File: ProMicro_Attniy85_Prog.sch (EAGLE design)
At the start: 4 parts, among them U1 ATTINY85-20P

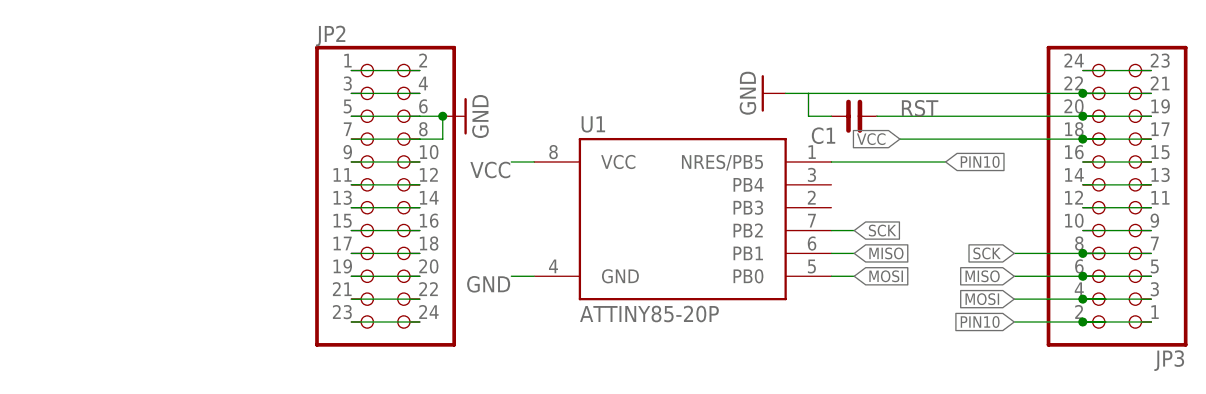
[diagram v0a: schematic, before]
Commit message: Add files via upload
LEDs added following the desing in [Utiliza tu placa Arduino como programador para ATtiny]https://fabricadigital.org/tutoriales/utiliza-tu-placa-arduino-como-programador-para-attiny/
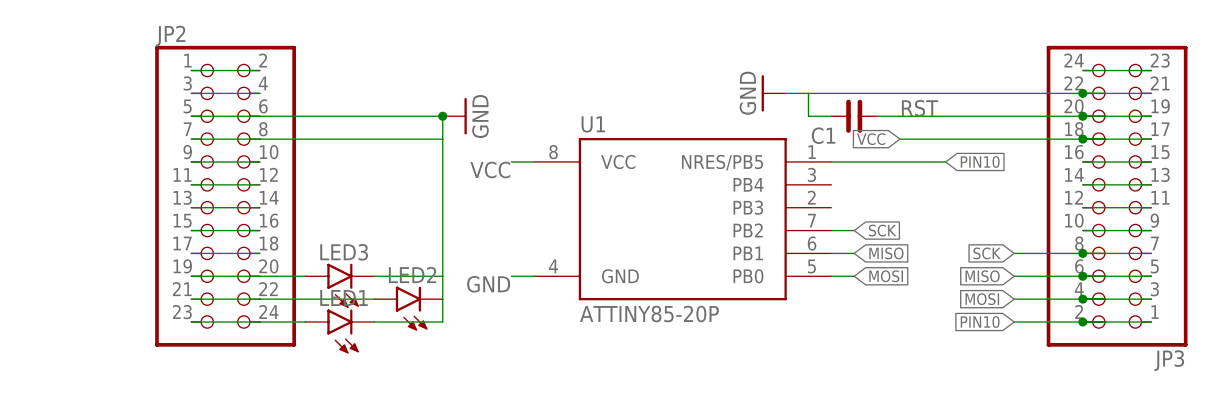
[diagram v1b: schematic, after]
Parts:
- added LED1, LED2, LED3: (no value), led:LEDCHIP-LED0805
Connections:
- removed net N$10: JP2.23, JP2.24
- removed net N$8: JP2.19, JP2.20
- removed net N$9: JP2.21, JP2.22
- new net PIN7: JP2.19, JP2.20, LED3.A
- new net PIN8: JP2.21, JP2.22, LED2.A
- new net PIN9: JP2.23, JP2.24, LED1.A
- net GND: now also LED1.C, LED2.C, LED3.C
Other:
- moved on the sheet: JP2
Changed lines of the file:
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@@
 <part name="JP2" library="pinhead" library_urn="urn:adsk.eagle:library:325" deviceset="PINHD-2X12" device="" package3d_urn="urn:adsk.eagle:package:22420/2"/>
 <part name="JP3" library="pinhead" library_urn="urn:adsk.eagle:library:325" deviceset="PINHD-2X12" device="" package3d_urn="urn:adsk.eagle:package:22420/2"/>
+<part name="LED1" library="led" library_urn="urn:adsk.eagle:library:259" deviceset="LED" device="CHIP-LED0805" package3d_urn="urn:adsk.eagle:package:15818/2"/>
+<part name="LED2" library="led" library_urn="urn:adsk.eagle:library:259" deviceset="LED" device="CHIP-LED0805" package3d_urn="urn:adsk.eagle:package:15818/2"/>
+<part name="LED3" library="led" library_urn="urn:adsk.eagle:library:259" deviceset="LED" device="CHIP-LED0805" package3d_urn="urn:adsk.eagle:package:15818/2"/>
 </parts>
 <sheets>
@@
 <attribute name="VALUE" x="57.15" y="23.8125" size="1.778" layer="96"/>
 </instance>
-<instance part="JP2" gate="A" x="7.62" y="20.32" smashed="yes">
-<attribute name="NAME" x="1.27" y="36.195" size="1.778" layer="95"/>
-<attribute name="VALUE" x="1.27" y="0" size="1.778" layer="96"/>
+<instance part="JP2" gate="A" x="-10.16" y="20.32" smashed="yes">
+<attribute name="NAME" x="-16.51" y="36.195" size="1.778" layer="95"/>
+<attribute name="VALUE" x="-16.51" y="0" size="1.778" layer="96"/>
 </instance>
 <instance part="JP3" gate="A" x="91.44" y="17.78" smashed="yes" rot="R180">
 <attribute name="NAME" x="97.79" y="1.905" size="1.778" layer="95" rot="R180"/>
 <attribute name="VALUE" x="97.79" y="38.1" size="1.778" layer="96" rot="R180"/>
+</instance>
+<instance part="LED1" gate="G$1" x="2.54" y="5.08" smashed="yes" rot="R90">
+<attribute name="NAME" x="7.112" y="8.636" size="1.778" layer="95" rot="R180"/>
+<attribute name="VALUE" x="7.112" y="10.795" size="1.778" layer="96" rot="R180"/>
+</instance>
+<instance part="LED2" gate="G$1" x="10.16" y="7.62" smashed="yes" rot="R90">
+<attribute name="NAME" x="14.732" y="11.176" size="1.778" layer="95" rot="R180"/>
+<attribute name="VALUE" x="14.732" y="13.335" size="1.778" layer="96" rot="R180"/>
+</instance>
+<instance part="LED3" gate="G$1" x="2.54" y="10.16" smashed="yes" rot="R90">
+<attribute name="NAME" x="7.112" y="13.716" size="1.778" layer="95" rot="R180"/>
+<attribute name="VALUE" x="7.112" y="15.875" size="1.778" layer="96" rot="R180"/>
 </instance>
 </instances>
@@
 <net name="GND" class="0">
 <segment>
-<wire x1="12.7" y1="27.94" x2="15.24" y2="27.94" width="0.1524" layer="91"/>
+<wire x1="-5.08" y1="27.94" x2="15.24" y2="27.94" width="0.1524" layer="91"/>
 <wire x1="15.24" y1="27.94" x2="15.24" y2="25.4" width="0.1524" layer="91"/>
 <pinref part="GND2" gate="1" pin="GND"/>
@@
 <pinref part="JP2" gate="A" pin="6"/>
 <pinref part="JP2" gate="A" pin="8"/>
-<wire x1="12.7" y1="25.4" x2="15.24" y2="25.4" width="0.1524" layer="91"/>
+<wire x1="-5.08" y1="25.4" x2="15.24" y2="25.4" width="0.1524" layer="91"/>
 <pinref part="JP2" gate="A" pin="5"/>
-<wire x1="5.08" y1="27.94" x2="12.7" y2="27.94" width="0.1524" layer="91"/>
+<wire x1="-12.7" y1="27.94" x2="-5.08" y2="27.94" width="0.1524" layer="91"/>
 <pinref part="JP2" gate="A" pin="7"/>
-<wire x1="5.08" y1="25.4" x2="12.7" y2="25.4" width="0.1524" layer="91"/>
+<wire x1="-12.7" y1="25.4" x2="-5.08" y2="25.4" width="0.1524" layer="91"/>
+<pinref part="LED1" gate="G$1" pin="C"/>
+<wire x1="7.62" y1="5.08" x2="15.24" y2="5.08" width="0.1524" layer="91"/>
+<pinref part="LED2" gate="G$1" pin="C"/>
+<wire x1="15.24" y1="5.08" x2="15.24" y2="7.62" width="0.1524" layer="91"/>
+<wire x1="15.24" y1="7.62" x2="15.24" y2="10.16" width="0.1524" layer="91"/>
+<pinref part="LED3" gate="G$1" pin="C"/>
+<wire x1="15.24" y1="10.16" x2="7.62" y2="10.16" width="0.1524" layer="91"/>
+<wire x1="15.24" y1="25.4" x2="15.24" y2="10.16" width="0.1524" layer="91"/>
 </segment>
 <segment>
@@
 <pinref part="JP2" gate="A" pin="2"/>
 <pinref part="JP2" gate="A" pin="1"/>
-<wire x1="12.7" y1="33.02" x2="5.08" y2="33.02" width="0.1524" layer="91"/>
+<wire x1="-5.08" y1="33.02" x2="-12.7" y2="33.02" width="0.1524" layer="91"/>
 </segment>
 </net>
@@
 <pinref part="JP2" gate="A" pin="3"/>
 <pinref part="JP2" gate="A" pin="4"/>
-<wire x1="5.08" y1="30.48" x2="12.7" y2="30.48" width="0.1524" layer="91"/>
+<wire x1="-12.7" y1="30.48" x2="-5.08" y2="30.48" width="0.1524" layer="91"/>
 </segment>
 </net>
@@
 <pinref part="JP2" gate="A" pin="9"/>
 <pinref part="JP2" gate="A" pin="10"/>
-<wire x1="5.08" y1="22.86" x2="12.7" y2="22.86" width="0.1524" layer="91"/>
+<wire x1="-12.7" y1="22.86" x2="-5.08" y2="22.86" width="0.1524" layer="91"/>
 </segment>
 </net>
@@
 <pinref part="JP2" gate="A" pin="11"/>
 <pinref part="JP2" gate="A" pin="12"/>
-<wire x1="5.08" y1="20.32" x2="12.7" y2="20.32" width="0.1524" layer="91"/>
+<wire x1="-12.7" y1="20.32" x2="-5.08" y2="20.32" width="0.1524" layer="91"/>
 </segment>
 </net>
@@
 <pinref part="JP2" gate="A" pin="13"/>
 <pinref part="JP2" gate="A" pin="14"/>
-<wire x1="5.08" y1="17.78" x2="12.7" y2="17.78" width="0.1524" layer="91"/>
+<wire x1="-12.7" y1="17.78" x2="-5.08" y2="17.78" width="0.1524" layer="91"/>
 </segment>
 </net>
@@
 <pinref part="JP2" gate="A" pin="15"/>
 <pinref part="JP2" gate="A" pin="16"/>
-<wire x1="5.08" y1="15.24" x2="12.7" y2="15.24" width="0.1524" layer="91"/>
+<wire x1="-12.7" y1="15.24" x2="-5.08" y2="15.24" width="0.1524" layer="91"/>
 </segment>
 </net>
@@
 <pinref part="JP2" gate="A" pin="17"/>
 <pinref part="JP2" gate="A" pin="18"/>
-<wire x1="5.08" y1="12.7" x2="12.7" y2="12.7" width="0.1524" layer="91"/>
-</segment>
-</net>
-<net name="N$8" class="0">
+<wire x1="-12.7" y1="12.7" x2="-5.08" y2="12.7" width="0.1524" layer="91"/>
+</segment>
+</net>
+<net name="PIN7" class="0">
 <segment>
 <pinref part="JP2" gate="A" pin="19"/>
 <pinref part="JP2" gate="A" pin="20"/>
-<wire x1="5.08" y1="10.16" x2="12.7" y2="10.16" width="0.1524" layer="91"/>
-</segment>
-</net>
-<net name="N$9" class="0">
+<wire x1="-12.7" y1="10.16" x2="-5.08" y2="10.16" width="0.1524" layer="91"/>
+<pinref part="LED3" gate="G$1" pin="A"/>
+<wire x1="0" y1="10.16" x2="-5.08" y2="10.16" width="0.1524" layer="91"/>
+</segment>
+</net>
+<net name="PIN8" class="0">
 <segment>
 <pinref part="JP2" gate="A" pin="21"/>
 <pinref part="JP2" gate="A" pin="22"/>
-<wire x1="5.08" y1="7.62" x2="12.7" y2="7.62" width="0.1524" layer="91"/>
-</segment>
-</net>
-<net name="N$10" class="0">
+<wire x1="-12.7" y1="7.62" x2="-5.08" y2="7.62" width="0.1524" layer="91"/>
+<pinref part="LED2" gate="G$1" pin="A"/>
+<wire x1="7.62" y1="7.62" x2="-5.08" y2="7.62" width="0.1524" layer="91"/>
+</segment>
+</net>
+<net name="PIN9" class="0">
 <segment>
 <pinref part="JP2" gate="A" pin="23"/>
 <pinref part="JP2" gate="A" pin="24"/>
-<wire x1="5.08" y1="5.08" x2="12.7" y2="5.08" width="0.1524" layer="91"/>
-</segment>
-</net>
+<wire x1="-12.7" y1="5.08" x2="-5.08" y2="5.08" width="0.1524" layer="91"/>
+<pinref part="LED1" gate="G$1" pin="A"/>
+<wire x1="0" y1="5.08" x2="-5.08" y2="5.08" width="0.1524" layer="91"/>
+</segment>
+</net>

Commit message: Add files via upload
minor changes
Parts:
- added R1, R2, R3: (no value), rc-master-smd:R_0805
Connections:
- new net N$10: LED1.A, R3.2
- new net N$8: LED3.A, R1.2
- new net N$9: LED2.A, R2.2
- net PIN7: now also R1.1; no longer LED3.A
- net PIN8: now also R2.1; no longer LED2.A
- net PIN9: now also R3.1; no longer LED1.A
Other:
- moved on the sheet: JP2
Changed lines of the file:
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@@
 <part name="LED2" library="led" library_urn="urn:adsk.eagle:library:259" deviceset="LED" device="CHIP-LED0805" package3d_urn="urn:adsk.eagle:package:15818/2"/>
 <part name="LED3" library="led" library_urn="urn:adsk.eagle:library:259" deviceset="LED" device="CHIP-LED0805" package3d_urn="urn:adsk.eagle:package:15818/2"/>
+<part name="R1" library="rc-master-smd" deviceset="R_" device="0805"/>
+<part name="R2" library="rc-master-smd" deviceset="R_" device="0805"/>
+<part name="R3" library="rc-master-smd" deviceset="R_" device="0805"/>
 </parts>
 <sheets>
@@
 <attribute name="VALUE" x="57.15" y="23.8125" size="1.778" layer="96"/>
 </instance>
-<instance part="JP2" gate="A" x="-10.16" y="20.32" smashed="yes">
-<attribute name="NAME" x="-16.51" y="36.195" size="1.778" layer="95"/>
-<attribute name="VALUE" x="-16.51" y="0" size="1.778" layer="96"/>
+<instance part="JP2" gate="A" x="-25.4" y="20.32" smashed="yes">
+<attribute name="NAME" x="-31.75" y="36.195" size="1.778" layer="95"/>
+<attribute name="VALUE" x="-31.75" y="0" size="1.778" layer="96"/>
 </instance>
 <instance part="JP3" gate="A" x="91.44" y="17.78" smashed="yes" rot="R180">
@@
 <attribute name="NAME" x="7.112" y="13.716" size="1.778" layer="95" rot="R180"/>
 <attribute name="VALUE" x="7.112" y="15.875" size="1.778" layer="96" rot="R180"/>
+</instance>
+<instance part="R1" gate="G$1" x="-10.16" y="10.16" smashed="yes">
+<attribute name="NAME" x="-12.7" y="11.7475" size="1.778" layer="95"/>
+<attribute name="VALUE" x="-12.7" y="6.985" size="1.778" layer="96"/>
+</instance>
+<instance part="R2" gate="G$1" x="-10.16" y="7.62" smashed="yes">
+<attribute name="NAME" x="-12.7" y="9.2075" size="1.778" layer="95"/>
+<attribute name="VALUE" x="-12.7" y="4.445" size="1.778" layer="96"/>
+</instance>
+<instance part="R3" gate="G$1" x="-10.16" y="5.08" smashed="yes">
+<attribute name="NAME" x="-12.7" y="6.6675" size="1.778" layer="95"/>
+<attribute name="VALUE" x="-12.7" y="1.905" size="1.778" layer="96"/>
 </instance>
 </instances>
@@
 <net name="GND" class="0">
 <segment>
-<wire x1="-5.08" y1="27.94" x2="15.24" y2="27.94" width="0.1524" layer="91"/>
+<wire x1="-20.32" y1="27.94" x2="15.24" y2="27.94" width="0.1524" layer="91"/>
 <wire x1="15.24" y1="27.94" x2="15.24" y2="25.4" width="0.1524" layer="91"/>
 <pinref part="GND2" gate="1" pin="GND"/>
@@
 <pinref part="JP2" gate="A" pin="6"/>
 <pinref part="JP2" gate="A" pin="8"/>
-<wire x1="-5.08" y1="25.4" x2="15.24" y2="25.4" width="0.1524" layer="91"/>
+<wire x1="-20.32" y1="25.4" x2="15.24" y2="25.4" width="0.1524" layer="91"/>
 <pinref part="JP2" gate="A" pin="5"/>
-<wire x1="-12.7" y1="27.94" x2="-5.08" y2="27.94" width="0.1524" layer="91"/>
+<wire x1="-27.94" y1="27.94" x2="-20.32" y2="27.94" width="0.1524" layer="91"/>
 <pinref part="JP2" gate="A" pin="7"/>
-<wire x1="-12.7" y1="25.4" x2="-5.08" y2="25.4" width="0.1524" layer="91"/>
+<wire x1="-27.94" y1="25.4" x2="-20.32" y2="25.4" width="0.1524" layer="91"/>
 <pinref part="LED1" gate="G$1" pin="C"/>
 <wire x1="7.62" y1="5.08" x2="15.24" y2="5.08" width="0.1524" layer="91"/>
@@
 <pinref part="JP2" gate="A" pin="2"/>
 <pinref part="JP2" gate="A" pin="1"/>
-<wire x1="-5.08" y1="33.02" x2="-12.7" y2="33.02" width="0.1524" layer="91"/>
+<wire x1="-20.32" y1="33.02" x2="-27.94" y2="33.02" width="0.1524" layer="91"/>
 </segment>
 </net>
@@
 <pinref part="JP2" gate="A" pin="3"/>
 <pinref part="JP2" gate="A" pin="4"/>
-<wire x1="-12.7" y1="30.48" x2="-5.08" y2="30.48" width="0.1524" layer="91"/>
+<wire x1="-27.94" y1="30.48" x2="-20.32" y2="30.48" width="0.1524" layer="91"/>
 </segment>
 </net>
@@
 <pinref part="JP2" gate="A" pin="9"/>
 <pinref part="JP2" gate="A" pin="10"/>
-<wire x1="-12.7" y1="22.86" x2="-5.08" y2="22.86" width="0.1524" layer="91"/>
+<wire x1="-27.94" y1="22.86" x2="-20.32" y2="22.86" width="0.1524" layer="91"/>
 </segment>
 </net>
@@
 <pinref part="JP2" gate="A" pin="11"/>
 <pinref part="JP2" gate="A" pin="12"/>
-<wire x1="-12.7" y1="20.32" x2="-5.08" y2="20.32" width="0.1524" layer="91"/>
+<wire x1="-27.94" y1="20.32" x2="-20.32" y2="20.32" width="0.1524" layer="91"/>
 </segment>
 </net>
@@
 <pinref part="JP2" gate="A" pin="13"/>
 <pinref part="JP2" gate="A" pin="14"/>
-<wire x1="-12.7" y1="17.78" x2="-5.08" y2="17.78" width="0.1524" layer="91"/>
+<wire x1="-27.94" y1="17.78" x2="-20.32" y2="17.78" width="0.1524" layer="91"/>
 </segment>
 </net>
@@
 <pinref part="JP2" gate="A" pin="15"/>
 <pinref part="JP2" gate="A" pin="16"/>
-<wire x1="-12.7" y1="15.24" x2="-5.08" y2="15.24" width="0.1524" layer="91"/>
+<wire x1="-27.94" y1="15.24" x2="-20.32" y2="15.24" width="0.1524" layer="91"/>
 </segment>
 </net>
@@
 <pinref part="JP2" gate="A" pin="17"/>
 <pinref part="JP2" gate="A" pin="18"/>
-<wire x1="-12.7" y1="12.7" x2="-5.08" y2="12.7" width="0.1524" layer="91"/>
+<wire x1="-27.94" y1="12.7" x2="-20.32" y2="12.7" width="0.1524" layer="91"/>
 </segment>
 </net>
@@
 <pinref part="JP2" gate="A" pin="19"/>
 <pinref part="JP2" gate="A" pin="20"/>
-<wire x1="-12.7" y1="10.16" x2="-5.08" y2="10.16" width="0.1524" layer="91"/>
-<pinref part="LED3" gate="G$1" pin="A"/>
-<wire x1="0" y1="10.16" x2="-5.08" y2="10.16" width="0.1524" layer="91"/>
+<wire x1="-27.94" y1="10.16" x2="-20.32" y2="10.16" width="0.1524" layer="91"/>
+<wire x1="-15.24" y1="10.16" x2="-20.32" y2="10.16" width="0.1524" layer="91"/>
+<pinref part="R1" gate="G$1" pin="1"/>
 </segment>
 </net>
@@
 <pinref part="JP2" gate="A" pin="21"/>
 <pinref part="JP2" gate="A" pin="22"/>
-<wire x1="-12.7" y1="7.62" x2="-5.08" y2="7.62" width="0.1524" layer="91"/>
-<pinref part="LED2" gate="G$1" pin="A"/>
-<wire x1="7.62" y1="7.62" x2="-5.08" y2="7.62" width="0.1524" layer="91"/>
+<wire x1="-27.94" y1="7.62" x2="-20.32" y2="7.62" width="0.1524" layer="91"/>
+<wire x1="-15.24" y1="7.62" x2="-20.32" y2="7.62" width="0.1524" layer="91"/>
+<pinref part="R2" gate="G$1" pin="1"/>
 </segment>
 </net>
@@
 <pinref part="JP2" gate="A" pin="23"/>
 <pinref part="JP2" gate="A" pin="24"/>
-<wire x1="-12.7" y1="5.08" x2="-5.08" y2="5.08" width="0.1524" layer="91"/>
-<pinref part="LED1" gate="G$1" pin="A"/>
-<wire x1="0" y1="5.08" x2="-5.08" y2="5.08" width="0.1524" layer="91"/>
+<wire x1="-27.94" y1="5.08" x2="-20.32" y2="5.08" width="0.1524" layer="91"/>
+<wire x1="-15.24" y1="5.08" x2="-20.32" y2="5.08" width="0.1524" layer="91"/>
+<pinref part="R3" gate="G$1" pin="1"/>
 </segment>
 </net>
@@
 </segment>
 </net>
+<net name="N$8" class="0">
+<segment>
+<pinref part="LED3" gate="G$1" pin="A"/>
+<wire x1="0" y1="10.16" x2="-5.08" y2="10.16" width="0.1524" layer="91"/>
+<pinref part="R1" gate="G$1" pin="2"/>
+</segment>
+</net>
+<net name="N$9" class="0">
+<segment>
+<pinref part="LED2" gate="G$1" pin="A"/>
+<wire x1="7.62" y1="7.62" x2="-5.08" y2="7.62" width="0.1524" layer="91"/>
+<pinref part="R2" gate="G$1" pin="2"/>
+</segment>
+</net>
+<net name="N$10" class="0">
+<segment>
+<pinref part="LED1" gate="G$1" pin="A"/>
+<wire x1="0" y1="5.08" x2="-5.08" y2="5.08" width="0.1524" layer="91"/>
+<pinref part="R3" gate="G$1" pin="2"/>
+</segment>
+</net>

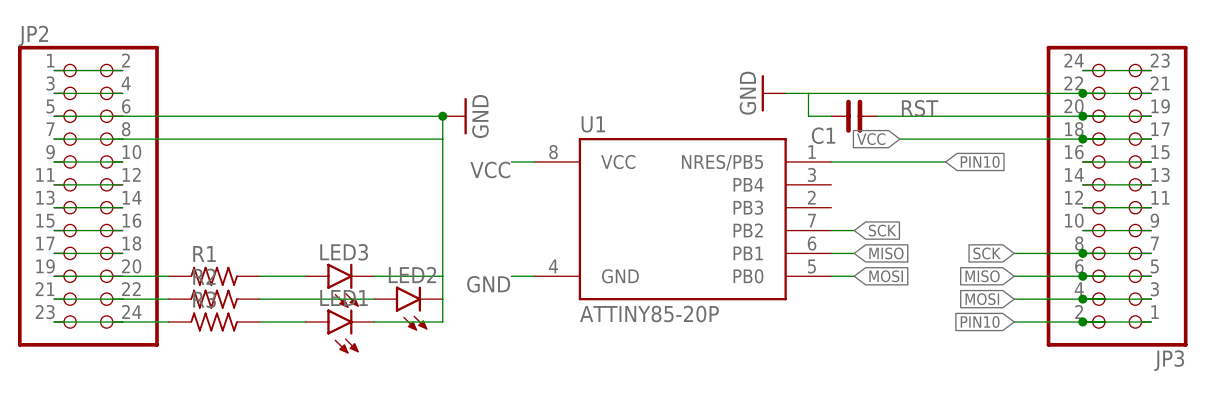
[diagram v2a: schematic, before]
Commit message: Add files via upload
As a recommendation from the AttinyCore85 Documentation, I've exchanged the capacitor (that was low) to an tantalum polar 100uf, and added another one of 0.1uf as coupler.
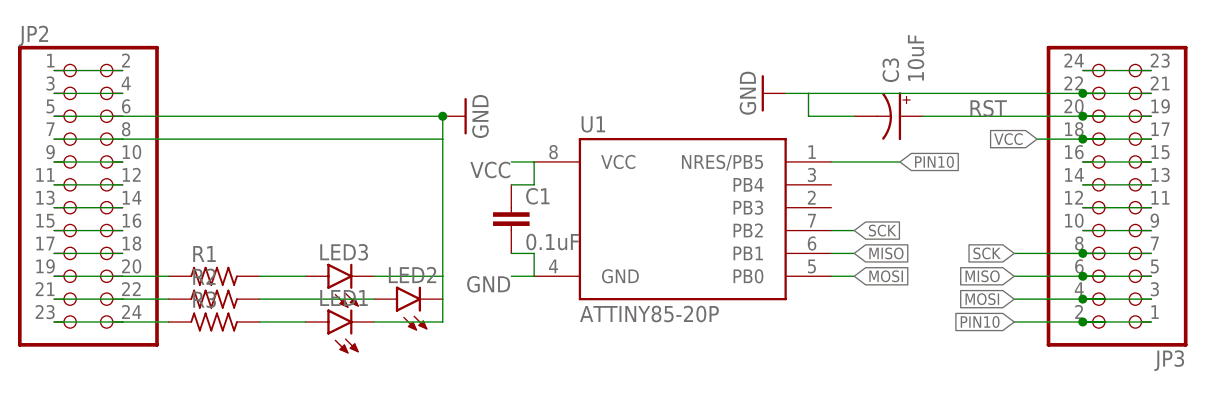
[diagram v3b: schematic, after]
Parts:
- added C3: 10uF, SparkFun-Capacitors:10UF-POLAR-EIA3216-16V-10%(TANT)
- C1: value (none) -> 0.1uF; device rc-master-smd:C_0805 -> SparkFun-Capacitors:0.1UF-0603-100V-10%
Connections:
- net GND: now also C1.2, C3.-; no longer C1.1
- net RST: now also C3.+; no longer C1.2
- net VCC: now also C1.1
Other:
- moved on the sheet: C1
